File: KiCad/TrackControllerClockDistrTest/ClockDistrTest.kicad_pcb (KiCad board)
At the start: 2 copper layers, 54 parts, among them J1 Conn_01x02_Male, J10 Conn_01x02_Male, J11 Conn_01x02_Male, J12 Conn_01x02_Male, J2 Conn_01x02_Male, J3 Conn_01x02_Male, J4 Conn_01x02_Male, J5 Conn_01x02_Male, J6 Conn_01x02_Male, J7 Conn_01x02_Male, J8 Conn_01x02_Male, J9 Conn_01x02_Male, U1 4049, U2 NB3N511, U3 LM7805_TO220, U4 MAX14783E, U5 MAX3284E, U6 MAX3284E, U7 MAX3284E, U8 MAX3284E, U9 MAX14783E, X1 SG-531, Y1 Crystal, Y2 Crystal

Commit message: Update ClockDistrTest.sch, had symbol update?
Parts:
- added J13: Conn_01x02_Male, Connector_PinHeader_2.54mm:PinHeader_1x02_P2.54mm_Vertical, F.Cu at (114.3, 132.1)
- added J14: Conn_01x02_Male, Connector_PinHeader_2.54mm:PinHeader_1x02_P2.54mm_Vertical, F.Cu at (129.5, 124.5)
- added J15: Conn_01x02_Male, Connector_PinHeader_2.54mm:PinHeader_1x02_P2.54mm_Vertical, F.Cu at (129.5, 132.1)
- added J16: Conn_01x02_Male, Connector_PinHeader_2.54mm:PinHeader_1x02_P2.54mm_Vertical, F.Cu at (142.2, 124.5)
- added J17: Conn_01x02_Male, Connector_PinHeader_2.54mm:PinHeader_1x02_P2.54mm_Vertical, F.Cu at (142.2, 132.1)
- added J18: Conn_01x02_Male, Connector_PinHeader_2.54mm:PinHeader_1x02_P2.54mm_Vertical, F.Cu at (154.9, 124.5)
- added J19: Conn_01x02_Male, Connector_PinHeader_2.54mm:PinHeader_1x02_P2.54mm_Vertical, F.Cu at (154.9, 132.1)
- added J20: Conn_01x02_Male, Connector_PinHeader_2.54mm:PinHeader_1x02_P2.54mm_Vertical, F.Cu at (167.6, 124.5)
- added J21: Conn_01x02_Male, Connector_PinHeader_2.54mm:PinHeader_1x02_P2.54mm_Vertical, F.Cu at (167.6, 132.1)
- added J22: Conn_01x02_Male, Connector_PinHeader_2.54mm:PinHeader_1x02_P2.54mm_Vertical, F.Cu at (180.3, 132.1)
- moved C14 118.7 mm to (137.2, 66.0), turned to 90 degrees
- moved J8 113.7 mm to (144.2, 53.3), turned to 270 degrees
- moved U6 112.4 mm to (142.2, 65.8), turned to 270 degrees
- moved J12 109.6 mm to (180.3, 53.3), turned to 90 degrees
- moved J1 96.7 mm to (83.8, 132.1), turned to 270 degrees
- moved R10 96.4 mm to (175.1, 66.8), turned to 180 degrees
- moved D1 96.1 mm to (88.9, 132.1)
- moved U9 95.5 mm to (181.5, 69.3), turned to 270 degrees
- moved C17 91.2 mm to (175.1, 70.6), turned to 180 degrees
- moved J10 83.8 mm to (156.9, 53.3), turned to 270 degrees
- moved C15 82.1 mm to (149.9, 66.0), turned to 90 degrees
- moved R7 80.7 mm to (185.4, 121.9)
- moved C16 80.1 mm to (162.6, 66.0), turned to 90 degrees
- moved U3 77.7 mm to (99.1, 124.5), turned to 90 degrees
- moved J9 76.6 mm to (131.5, 53.3), turned to 270 degrees
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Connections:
- R4 pad 1: A -> /RS422-B
- R5 pad 1: B -> Net-(J13-Pad1)
- R5 pad 2: A -> /RS422-B
- R6 pad 2: B -> Net-(J13-Pad1)
- R7 pad 1: A -> Net-(J22-Pad2)
- R8 pad 1: B -> Net-(J22-Pad1)
- R8 pad 2: A -> Net-(J22-Pad2)
- R9 pad 2: B -> Net-(J22-Pad1)
- U4 pad 6: B -> Net-(J13-Pad1)
- U4 pad 7: A -> /RS422-B
- U5 pad 4: B -> B1
- U5 pad 6: A -> A1
- U6 pad 4: B -> B2
- U6 pad 6: A -> A2
- U7 pad 4: B -> B3
- U7 pad 6: A -> A3
- U8 pad 4: B -> B4
- U8 pad 6: A -> A4
- U9 pad 6: B -> Net-(J22-Pad1)
- U9 pad 7: A -> Net-(J22-Pad2)
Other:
- board outline added: 111.8 x 88.9 mm

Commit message: intermediate update on schematic
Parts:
- added C18: 22u, Capacitor_SMD:C_1206_3216Metric, F.Cu at (135.9, 90.4)
- added C19: 0.1u, Capacitor_SMD:C_1206_3216Metric, F.Cu at (135.9, 96.2)
- added C20: 0.1u, Capacitor_SMD:C_1206_3216Metric, F.Cu at (140.9, 90.4)
- added C21: 22u, Capacitor_SMD:C_1206_3216Metric, F.Cu at (135.9, 101.9)
- added C22: 22u, Capacitor_SMD:C_1206_3216Metric, F.Cu at (145.9, 90.4)
- added C23: 0.1u, Capacitor_SMD:C_1206_3216Metric, F.Cu at (140.9, 96.2)
- added C24: 0.1u, Capacitor_SMD:C_1206_3216Metric, F.Cu at (145.9, 96.2)
- added C25: 22u, Capacitor_SMD:C_1206_3216Metric, F.Cu at (140.9, 101.9)
- added C26: 0.1u, Capacitor_SMD:C_1206_3216Metric, F.Cu at (151.0, 90.4)
- added R12: 1K, Resistor_SMD:R_1206_3216Metric, F.Cu at (145.9, 101.9)
- added R13: 10E, Resistor_SMD:R_1206_3216Metric, F.Cu at (156.0, 90.4)
- added R14: 10E, Resistor_SMD:R_1206_3216Metric, F.Cu at (151.0, 96.2)
- added R15: 1K, Resistor_SMD:R_1206_3216Metric, F.Cu at (156.0, 96.2)
- added R16: 120E, Resistor_SMD:R_1206_3216Metric, F.Cu at (151.0, 101.9)
- added R17: 1K, Resistor_SMD:R_1206_3216Metric, F.Cu at (161.0, 90.4)
- added R18: 10E, Resistor_SMD:R_1206_3216Metric, F.Cu at (156.0, 101.9)
- C1: value C -> 12p
- C10, C5: value C -> 10pF
- C15, C17, C2: value C -> 22u
- C16, C4, C7: value C -> 0.1u
- C3: value 10pF -> 12p
- C6: value 10pF -> 22u
- R1: value 1M -> 10E
- R11: value 300 -> 120E
- R2: value 270 -> 10E
- R3: value 1K -> 1M
- R4: value 1K -> 270
- R5, R8: value 120E -> 10E
- R6: value 1K -> 300
- R7, R9: value 1K -> 10E
- moved R10 4.47 mm to (174.0, 71.1), turned to 270 degrees
- moved C17 1.51 mm to (176.5, 71.1), turned to 270 degrees
- moved C13 1.27 mm to (125.7, 66.0)
- moved C14 1.27 mm to (138.4, 66.0)
- moved C16 1.27 mm to (163.8, 66.0)
- moved J14 1.27 mm to (130.8, 124.5)
- moved J15 1.27 mm to (130.8, 132.1)
- moved J18 1.27 mm to (156.2, 124.5)
- moved J19 1.27 mm to (156.2, 132.1)
- moved J20 1.27 mm to (168.9, 124.5)
- moved J21 1.27 mm to (168.9, 132.1)
- moved J13 1.27 mm to (115.6, 132.1)
- moved J16 1.27 mm to (143.5, 124.5)
- moved J17 1.27 mm to (143.5, 132.1)
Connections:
- C10 pad 1: +5V -> Net-(C10-Pad1)
- C11 pad 1: +5V -> Net-(C11-Pad1)
- C12 pad 1: +5V -> Net-(C11-Pad1)
- C15 pad 1: +5V -> Net-(C15-Pad1)
- C16 pad 1: +5V -> Net-(C15-Pad1)
- C17 pad 1: +5V -> Net-(C17-Pad1)
- C4 pad 1: Net-(C4-Pad1) -> Net-(C2-Pad1)
- C5 pad 1: Net-(C4-Pad1) -> Net-(C5-Pad1)
- C7 pad 1: +5V -> Net-(C6-Pad1)
- C8 pad 1: +5V -> Net-(C8-Pad1)
- C9 pad 1: +5V -> Net-(C8-Pad1)
- D1 pad 2: Net-(C4-Pad1) -> Net-(C8-Pad1)
- J10 pad 1: GND -> A1
- J10 pad 2: Net-(J10-Pad2) -> B1
- J11 pad 1: GND -> A2
- J11 pad 2: Net-(J11-Pad2) -> B2
- J12 pad 1: GND -> A2
- J12 pad 2: Net-(J12-Pad2) -> B2
- J13 pad 1: Net-(J13-Pad1) -> A3
- J13 pad 2: /RS422-B -> B3
- J14 pad 1: A1 -> GND
- J14 pad 2: B1 -> Net-(J14-Pad2)
- J15 pad 1: A1 -> GND
- J15 pad 2: B1 -> Net-(J15-Pad2)
- J16 pad 1: A2 -> A3
- J16 pad 2: B2 -> B3
- J17 pad 1: A2 -> A4
- J17 pad 2: B2 -> B4
- J18 pad 1: A3 -> A4
- J18 pad 2: B3 -> B4
- J19 pad 1: A3 -> Net-(J19-Pad1)
- J19 pad 2: B3 -> Net-(J19-Pad2)
- J20 pad 1: A4 -> GND
- J20 pad 2: B4 -> Net-(J20-Pad2)
- J21 pad 1: A4 -> GND
- J21 pad 2: B4 -> Net-(J21-Pad2)
- J22 pad 1: Net-(J22-Pad1) -> GND
- J8 pad 1: GND -> Net-(J8-Pad1)
- J8 pad 2: Net-(J8-Pad2) -> /RS422-B
- J9 pad 1: GND -> A1
- J9 pad 2: Net-(J9-Pad2) -> B1
- R1 pad 1: Net-(R1-Pad1) -> +5V
- R1 pad 2: Net-(C3-Pad1) -> Net-(C2-Pad1)
- R10 pad 1: Net-(R10-Pad1) -> /RS422-B
- R10 pad 2: GND -> +5V
- R11 pad 1: +5V -> Net-(J8-Pad1)
- R11 pad 2: Net-(D2-Pad2) -> /RS422-B
- R2 pad 1: Net-(C6-Pad1) -> +5V
- R2 pad 2: Net-(R1-Pad1) -> Net-(C6-Pad1)
- R3 pad 2: +5V -> Net-(C5-Pad1)
- R4 pad 1: /RS422-B -> Net-(C10-Pad1)
- R4 pad 2: +5V -> Net-(R3-Pad1)
- R5 pad 1: Net-(J13-Pad1) -> Net-(C11-Pad1)
- R5 pad 2: /RS422-B -> +5V
- R6 pad 1: GND -> +5V
- R6 pad 2: Net-(J13-Pad1) -> Net-(D2-Pad2)
- R7 pad 1: Net-(J22-Pad2) -> Net-(C15-Pad1)
- R8 pad 1: Net-(J22-Pad1) -> +5V
- R8 pad 2: Net-(J22-Pad2) -> Net-(C17-Pad1)
- R9 pad 1: GND -> +5V
- R9 pad 2: Net-(J22-Pad1) -> Net-(C18-Pad1)
- U1 pad 1: +5V -> Net-(C2-Pad1)
- U1 pad 15: Net-(J2-Pad2) -> Net-(J3-Pad2)
- U1 pad 2: Net-(R1-Pad1) -> Net-(R3-Pad1)
- U1 pad 3: Net-(C3-Pad1) -> Net-(C5-Pad1)
- U1 pad 5: Net-(R1-Pad1) -> Net-(R3-Pad1)
- U2 pad 2: +5V -> Net-(C11-Pad1)
- U2 pad 7: +5V -> Net-(C11-Pad1)
- U2 pad 8: Net-(C2-Pad1) -> Net-(C3-Pad1)
- U3 pad 1: Net-(C4-Pad1) -> Net-(C8-Pad1)
- U4 pad 2: Net-(R3-Pad1) -> Net-(C15-Pad1)
- U4 pad 3: Net-(R3-Pad1) -> Net-(C15-Pad1)
- U4 pad 6: Net-(J13-Pad1) -> Net-(J8-Pad1)
- U4 pad 8: +5V -> Net-(C15-Pad1)
- U5 pad 1: +5V -> Net-(C17-Pad1)
- U5 pad 3: Net-(J9-Pad2) -> Net-(J15-Pad2)
- U5 pad 5: +5V -> Net-(C17-Pad1)
- U6 pad 1: +5V -> Net-(C18-Pad1)
- U6 pad 3: Net-(J8-Pad2) -> Net-(J14-Pad2)
- U6 pad 5: +5V -> Net-(C18-Pad1)
- U7 pad 1: +5V -> Net-(C21-Pad1)
- U7 pad 3: Net-(J10-Pad2) -> Net-(J20-Pad2)
- U7 pad 5: +5V -> Net-(C21-Pad1)
- U8 pad 1: +5V -> Net-(C22-Pad1)
- U8 pad 3: Net-(J11-Pad2) -> Net-(J21-Pad2)
- U8 pad 5: +5V -> Net-(C22-Pad1)
- U9 pad 1: Net-(J12-Pad2) -> Net-(J22-Pad2)
- U9 pad 2: Net-(R10-Pad1) -> GND
- U9 pad 3: Net-(R10-Pad1) -> GND
- U9 pad 6: Net-(J22-Pad1) -> Net-(J19-Pad1)
- U9 pad 7: Net-(J22-Pad2) -> Net-(J19-Pad2)
- U9 pad 8: +5V -> Net-(C25-Pad1)
- X1 pad 1: +5V -> Net-(C6-Pad1)
- X1 pad 5: Net-(J3-Pad2) -> Net-(J2-Pad2)
- X1 pad 8: +5V -> Net-(C6-Pad1)
- Y1 pad 2: Net-(C2-Pad1) -> Net-(C3-Pad1)
- Y2 pad 1: Net-(C6-Pad1) -> Net-(C10-Pad1)
- Y2 pad 2: Net-(C3-Pad1) -> Net-(C5-Pad1)

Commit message: Updated schematic
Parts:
- removed J5, J6, J7: Conn_01x02_Male, Connector_PinHeader_2.54mm:PinHeader_1x02_P2.54mm_Vertical
- moved J11 84.7 mm to (138.4, 132.1)
- moved R7 83.6 mm to (118.1, 72.4), turned to 0 degrees
- moved J12 82.5 mm to (138.4, 124.5), turned to 270 degrees
- moved R8 79.7 mm to (129.5, 66.0), turned to 180 degrees
- moved J9 78.9 mm to (125.7, 132.1)
- moved J15 78.8 mm to (127.0, 53.3)
- moved J22 78.8 mm to (176.5, 53.3)
- moved J21 78.8 mm to (166.4, 53.3)
- moved J10 77.6 mm to (125.7, 124.5)
- moved J8 77.6 mm to (113.0, 124.5), turned to 90 degrees
- moved J20 73.0 mm to (152.4, 53.3)
- moved J14 71.7 mm to (139.7, 53.3)
- moved C9 66.7 mm to (102.9, 123.2), turned to 90 degrees
- moved R9 66.2 mm to (142.2, 66.0), turned to 180 degrees
- moved C14 61.7 mm to (105.4, 118.1), turned to 270 degrees
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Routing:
- net GND: track 0.00 -> 172.2 mm, vias 0 -> 9
- net +5V: track 0.00 -> 123.5 mm
- net Net-(J8-Pad1): track 0.00 -> 56.1 mm, vias 0 -> 1
- net /RS422-B: track 0.00 -> 56.1 mm, vias 0 -> 1
- net Net-(J3-Pad2): track 0.00 -> 30.3 mm
- net Net-(C6-Pad1): track 0.00 -> 19.4 mm
- net Net-(C15-Pad1): track 0.00 -> 17.2 mm
- net Net-(U1-Pad11): track 0.00 -> 16.0 mm
- net Net-(R3-Pad1): track 0.00 -> 15.5 mm
- net Net-(J4-Pad2): track 0.00 -> 14.6 mm
- net Net-(C11-Pad1): track 0.00 -> 14.3 mm
- net Net-(C8-Pad1): track 0.00 -> 14.0 mm
- net Net-(J2-Pad1): track 0.00 -> 13.4 mm
- net Net-(C10-Pad1): track 0.00 -> 13.0 mm
- net Net-(C5-Pad1): track 0.00 -> 11.7 mm
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- added copper zone on B.Cu, net GND
- added copper zone on F.Cu, net GND

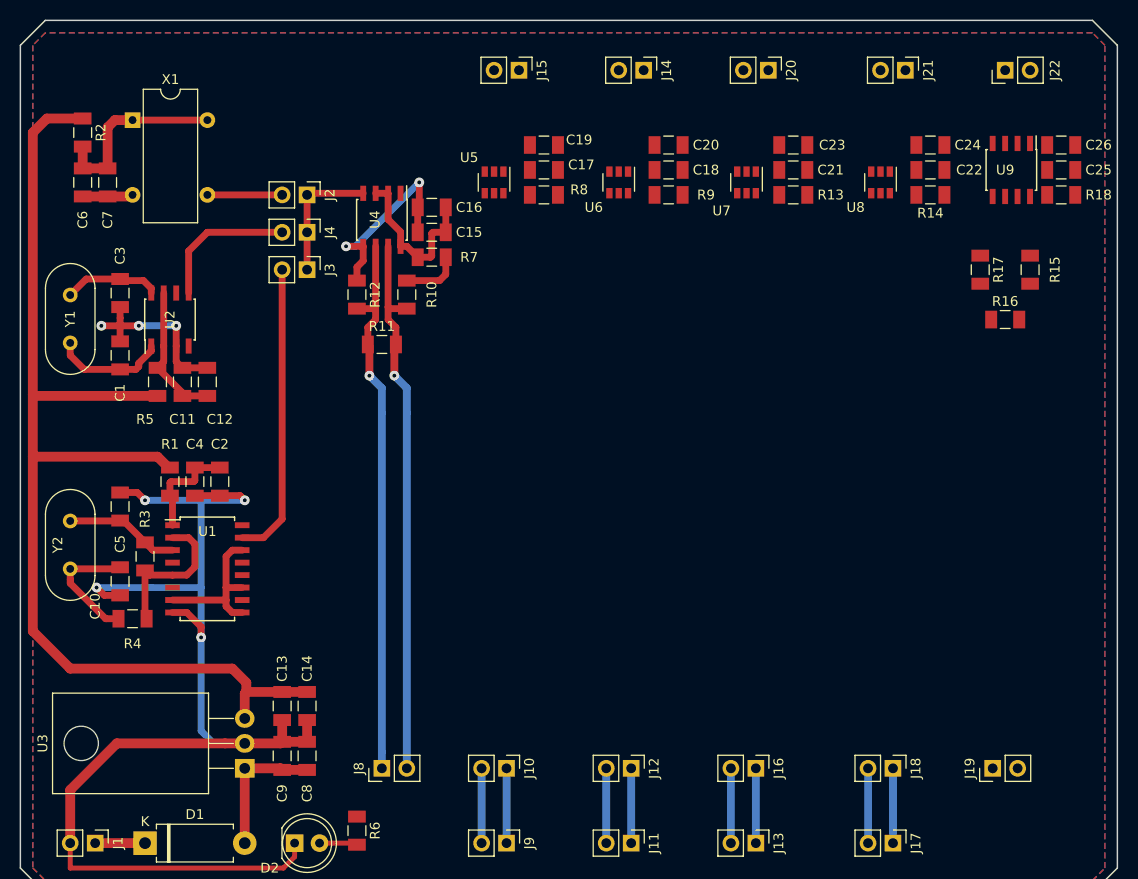
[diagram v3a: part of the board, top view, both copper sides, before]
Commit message: Finalized ClockDistrTest.sch generated plot files.
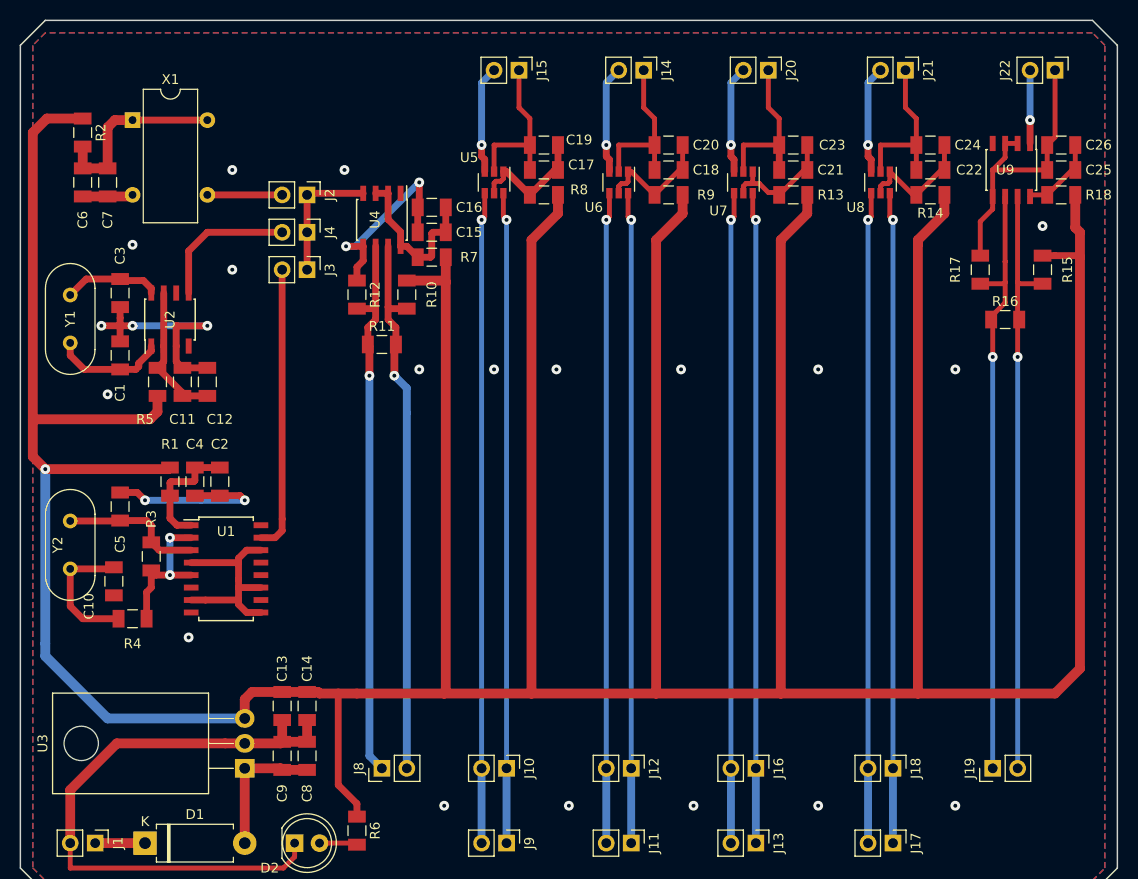
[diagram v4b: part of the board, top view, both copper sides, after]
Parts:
- moved J22 5.08 mm to (181.6, 53.3), turned to 270 degrees
- moved U1 1.91 mm to (97.2, 104.1)
- moved R15 1.27 mm to (180.3, 73.7)
- moved C10 0.64 mm to (85.7, 105.4)
- moved R3 0.63 mm to (89.5, 102.9)
- moved U7 0.32 mm to (149.9, 64.8)
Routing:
- net +5V: track 123.5 -> 520.4 mm, vias 0 -> 1
- net Net-(J19-Pad1): track 0.00 -> 61.5 mm, vias 0 -> 1
- net Net-(J19-Pad2): track 0.00 -> 61.0 mm, vias 0 -> 1
- net B2: track 7.62 -> 66.3 mm, vias 0 -> 1
- net B1: track 7.62 -> 66.3 mm, vias 0 -> 1
- net A1: track 7.62 -> 66.3 mm, vias 0 -> 1
- net B4: track 7.62 -> 66.3 mm, vias 0 -> 1
- net B3: track 7.62 -> 66.3 mm, vias 0 -> 1
- net A4: track 7.62 -> 66.3 mm, vias 0 -> 1
- net A3: track 7.62 -> 66.3 mm, vias 0 -> 1
- net A2: track 7.62 -> 66.3 mm, vias 0 -> 1
- net GND: track 172.2 -> 229.8 mm, vias 9 -> 25
- net Net-(C21-Pad1): track 0.00 -> 13.2 mm
- net Net-(C17-Pad1): track 0.00 -> 13.0 mm
- net Net-(C22-Pad1): track 0.00 -> 13.0 mm
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
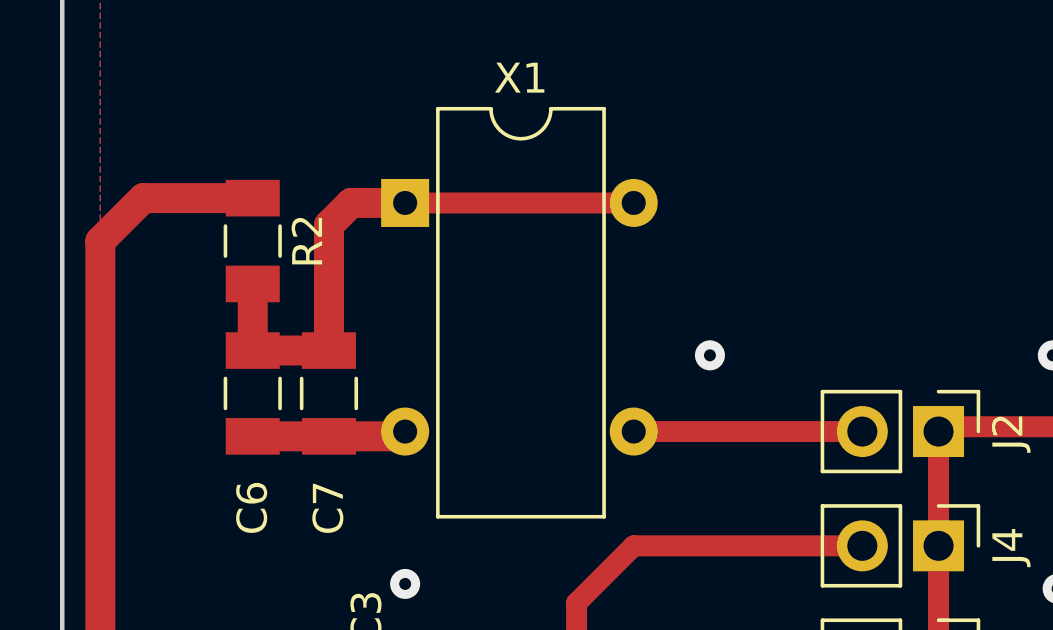
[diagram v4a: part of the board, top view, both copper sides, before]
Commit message: Update on CMOS clock IC, through hole non plated holes solder fix
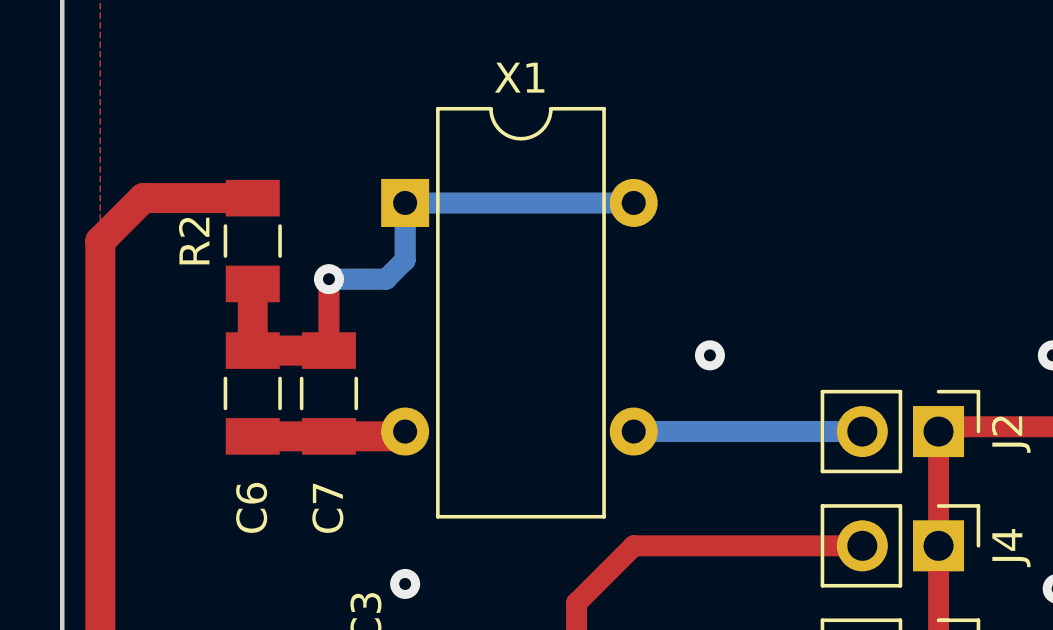
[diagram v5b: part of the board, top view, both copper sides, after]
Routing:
- net Net-(C6-Pad1): track 19.4 -> 19.5 mm, vias 0 -> 1
